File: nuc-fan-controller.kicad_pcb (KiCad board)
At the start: 2 copper layers, 124 x 85 mm, 42 parts, among them J1 19V IN, J2 NUC fan header, J3 FAN 1, J4 FAN 2, J5 Pro Mini, Q1 BC547B, Q2 BC547B, Q3 IRFZ44N, U1 LM2596T, U2 AMS1117-5.0, U3 AMS1117-3.3

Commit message: nuc-fan-controller: the 19V->12V converter is a module now, not parts on the board
Seven parts and their copper — U1 LM2596T-ADJ, L1 100 uH 6 A toroid, D1 1N5822,
C1 220u/35V, C2 100n, R1 1k, RV1 10k trim — are replaced by J6, a 1x04 header
(1,2 GND / 3 19V / 4 +12V) that a finished XL4016E1 step-down module from
cabinet L1 A10 plugs into. C3 470u/25V and C4 stay as the board's local
decoupling where the 12 V rail lands.

This reverses an earlier instruction: the XL4016E1 module had been ruled out and
the converter built from parts instead. The ruling is lifted. BUILD.md says so
out loud and carries the arithmetic that makes the module the better answer at
12 V / 1 A — 5-40 V in, 1.2-36 V out, 8 A, ~180 kHz, ~50 mV ripple; 0.16 A
inductor ripple at this load so it never enters discontinuous conduction and
never pulse-skips; 50 mV of rail ripple attenuated ~5000x by the PWM_IN
divider's time constant. The discrete design is in 10bc262 and every part of it
is still in the cabinet, so the swap goes both ways.

Schematic: 52 wires and 5 junctions, and they are exactly what logs/genwires.py
emits — logs/applywires.py is new and splices that set back into the .kicad_sch.
A pin or a name tag only connects to a wire END, so 19V is written as the segment
chain J1.1 -> (43.18,44.45) -> (48.26,44.45) -> J6.3, the vertices being where
the PWR_FLAG and the name tag hang off it; as one straight wire ERC reports both
as orphaned. ERC: 0 violations.

Board: J6 at (24,34); 19V routed J1 -> (18,34) -> (18,39.08) -> J6.3 and +12V
from J6.4 down and across onto the existing rail; the SW/FB/19V tracks, 22
dangling GND/+12V segments and one stray via deleted; zones refilled; the dead
SW netclass pattern removed; silkscreen beside J6 reads "1,2 GND 3 19V 4 12V".
DRC: 0 violations, 0 unconnected items, and the one documented parity warning —
J2 pin 4's deliberate no-connect.

exports/ rebuilt by logs/export.sh (new): BOM is 32 fitted parts, plus gerbers,
drill, placement, both board plots 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
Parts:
- removed C1: 220uF 35V, Capacitor_THT:CP_Radial_D10.0mm_P5.00mm
- removed C2: 100n, Capacitor_THT:C_Disc_D3.8mm_W2.6mm_P2.50mm
- removed D1: 1N5822, Diode_THT:D_DO-201AD_P15.24mm_Horizontal
- removed L1: 100uH 6A, Inductor_THT:L_Toroid_Horizontal_D16.8mm_P14.70mm_Vishay_TJ3
- removed R1: 1k, Resistor_THT:R_Axial_DIN0204_L3.6mm_D1.6mm_P5.08mm_Horizontal
- removed RV1: 10k trim, Potentiometer_THT:Potentiometer_Bourns_3296W_Vertical
- removed U1: LM2596T, Package_TO_SOT_THT:TO-220-5_P3.4x3.7mm_StaggerOdd_Lead3.8mm_Vertical
- added J6: BUCK MODULE, Connector_PinHeader_2.54mm:PinHeader_1x04_P2.54mm_Vertical, F.Cu at (24.0, 34.0)
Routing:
- net GND: track 333.3 -> 199.5 mm, vias 326 -> 325
- net SW: track 39.6 -> 0.00 mm
- net FB: track 24.5 -> 0.00 mm
- net +12V: track 147.3 -> 166.0 mm
- net 19V: track 31.7 -> 15.1 mm
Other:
- board text added: "1,2 GND 3 19V 4 12V"

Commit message: Wire Q1/Q2 for the BC547s that are actually in the cabinet
The two transistors in R1 D3 are the NXP/Philips order — 1 emitter, 2 base,
3 collector. KiCad's Transistor_BJT:BC547 is the onsemi order (1 C, 2 B, 3 E), so
the schematic, the footprint pad numbers and the parts disagreed. Both symbols are
now Transistor_BJT:Q_NPN_EBC, which draws at identical pin coordinates and differs
only in the pin numbers: nothing on the drawing moved, the nets moved.

schematic (logs/fixq.py)
  Q1/Q2 -> Q_NPN_EBC, Sim.Pins 1=E 2=B 3=C, and the Datasheet link plus the
  Description now state the pinning. ERC 0 violations.

board (logs/fixboard.py, fixboard2.py, fixboard3.py)
  Pad 1 is the emitter on the GND pour, pad 3 the collector. NUC_TACH is re-run
  from Q1 pad 3 around the body onto the tach line at (109.73,18.782); FAN_GATE
  from Q2 pad 3 east to the existing run at (102.969,77.1109). The copper that used
  to hang off the old pads is gone: the GND feeds off Q1.3/Q2.3, the stubs into
  Q1.1/Q2.1, and the orphaned GND feed into R7.2 — R7 takes GND from the pour.
  BASE is jogged to y=74.75 so it clears Q2's now-live pad 1 by 0.40 mm instead of
  0.20, and two stitching vias in the new corridors plus a +12V via with copper on
  one layer only were removed. Silkscreen between the transistors reads
  "Q1 Q2 1=E 2=B 3=C"; pad 1 is the square pad.
  DRC 0 violations, 0 unconnected items, and the documented J2 pin-4 no-connect.

Update-from-schematic also brought in J7 (FAN 1 — the third fan connector) and
C12 100 n on FAN_SW, which were in the schematic but not on the board. J7 sits in
the fan column at (130,76) and is routed with the same bypass style the J3/J4 legs
use. That update had renamed FAN_SW to Net-(C12-Pad1) and PWM_DIV to Net-(R3-Pad2)
on the board, which drops both out of the Power net class, so the names were put
back by hand. BOM is 33 fitted parts.

Docs: BUILD.md gains "Which way round a BC547 goes" — meter them, a BC547B reads
hFE 200-450 forward and single digit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
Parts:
- added J7: FAN 1, Connector_PinHeader_2.54mm:PinHeader_1x02_P2.54mm_Vertical, F.Cu at (130.0, 76.0)
- J3: value FAN 1 -> FAN 2
- J4: value FAN 2 -> FAN 3
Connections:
- Q1 pad 1: NUC_TACH -> GND
- Q1 pad 3: GND -> NUC_TACH
- Q2 pad 1: FAN_GATE -> GND
- Q2 pad 3: GND -> FAN_GATE
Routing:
- net GND: track 199.5 -> 169.4 mm, vias 325 -> 322
- net +12V: track 166.0 -> 182.0 mm
- net NUC_TACH: track 25.8 -> 39.6 mm
- net FAN_SW: track 51.9 -> 63.1 mm
- net FAN_GATE: track 19.7 -> 15.3 mm
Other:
- board text added: "Q1 Q2 1=E 2=B 3=C"

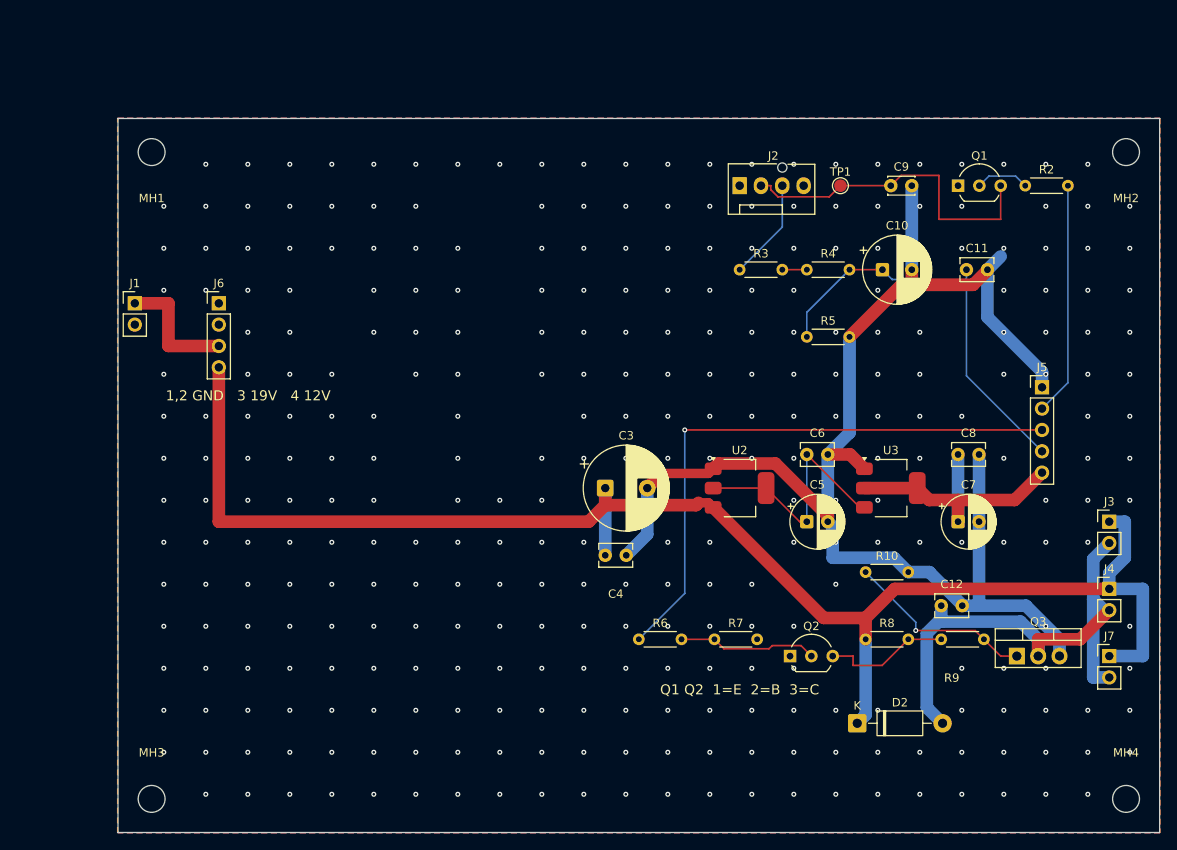
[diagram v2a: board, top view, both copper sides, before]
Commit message: Rebuild the board as one copper layer, 88.90 x 76.20 mm, for home etching
The board is now generated by logs/build1l.py instead of routed by Freerouting: parts,
drawn rails, holes, silkscreen and a small A* for the short legs all live in that script,
with footprint artwork cloned out of the KiCad 10 libraries by logs/getfp.py into
logs/fp-templates.inc.  logs/setrules.py writes the home-etch rules into the project.

Rules: clearance and minimum track 0.70 mm, drawn rails 1.80 mm, copper-to-edge 0.50 mm,
minimum drill 0.90 mm, maximum pad 1.80 mm, pour minimum thickness 0.80 mm.  Every layer
is F.Cu, and F.Cu is the component side, so the copper that gets etched is the copper the
parts solder to and nothing about the board is mirrored.

The ground pour is one island of 5009 mm2 with `connect_pads yes` -- the token matters:
KiCad 10 reads a bare `(connect_pads (clearance 0.7))` as thermal relief and stops the fill
0.70 mm short of every GND pad, which passes DRC and leaves the pads sitting in resin.
Traces of a foreign net keep the pour off, tracks of the pour's own net are absorbed by it,
which is why the router keeps a 2.20 mm gap (2 x clearance + min_thickness) between thin
copper so the fill never gets walled into pockets.

Nets that would fight each other are drawn as bars rather than handed to the router --
+12V, FAN_SW, 19V, +3V3, FAN_PWM, NUC_TACH, NUC_PWM, TACH_OUT, TACH_BASE, PWM_IN -- because
a long leg left to the A* escapes to the board perimeter and walls the pour off.  One
crossing cannot be routed around on a single layer: the Pro Mini's A0 and D11 sit side by
side and their destinations are on opposite sides of the divider row, so R11, a 0 Ohm
bridge, carries FAN_PWM over that row.  R11 is a board part only; the schematic has no such
component, and KiCad's board-only ratsnest therefore reports the join as a missing
connection, which is why that rule is downgraded to a warning and logs/verify.py checks the
real thing instead.

logs/verify.py and logs/p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
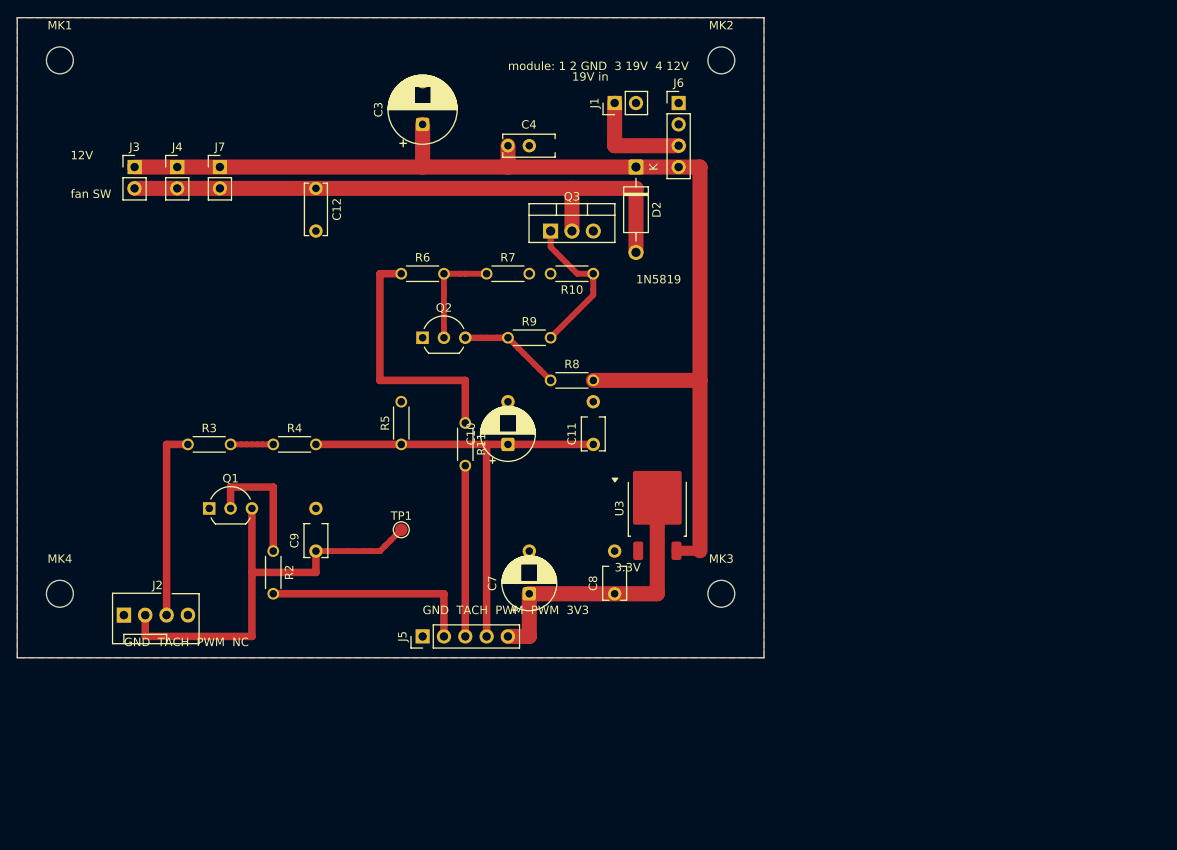
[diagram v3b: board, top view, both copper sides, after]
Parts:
- removed C5: 10uF, Capacitor_THT:CP_Radial_D6.3mm_P2.50mm
- removed C6: 100n, Capacitor_THT:C_Disc_D3.8mm_W2.6mm_P2.50mm
- removed MH1, MH2, MH3, MH4: MountingHole_3.2mm_M3, MountingHole:MountingHole_3.2mm_M3
- removed U2: AMS1117-5.0, Package_TO_SOT_SMD:SOT-223-3_TabPin2
- added MK1: M3, MountingHole:MountingHole_3.2mm_M3, F.Cu at (5.08, 5.08)
- added MK2: M3, MountingHole:MountingHole_3.2mm_M3, F.Cu at (83.8, 5.08)
- added MK3: M3, MountingHole:MountingHole_3.2mm_M3, F.Cu at (83.8, 68.6)
- added MK4: M3, MountingHole:MountingHole_3.2mm_M3, F.Cu at (5.08, 68.6)
- added R11: 0R bridge, Resistor_THT:R_Axial_DIN0204_L3.6mm_D1.6mm_P5.08mm_Horizontal, F.Cu at (53.3, 48.2)
- C10: footprint Capacitor_THT:CP_Radial_D8.0mm_P3.50mm -> Capacitor_THT:CP_Radial_D6.3mm_P2.50mm
- C12, C4: footprint Capacitor_THT:C_Disc_D3.8mm_W2.6mm_P2.50mm -> Capacitor_THT:C_Disc_D6.0mm_W2.5mm_P5.00mm
- C3: footprint Capacitor_THT:CP_Radial_D10.0mm_P5.00mm -> Capacitor_THT:CP_Radial_D8.0mm_P3.50mm
- C9: footprint Capacitor_THT:C_Disc_D3.0mm_W2.0mm_P2.50mm -> Capacitor_THT:C_Disc_D3.8mm_W2.6mm_P2.50mm
- U3: footprint Package_TO_SOT_SMD:SOT-223-3_TabPin2 -> Package_TO_SOT_SMD:TO-252-3_TabPin2
- moved J3 123.5 mm to (14.0, 17.8)
- moved J4 121.8 mm to (19.1, 17.8)
- moved J7 120.8 mm to (24.1, 17.8)
- moved R2 99.5 mm to (30.5, 63.5)
- moved Q1 97.1 mm to (22.9, 58.4)
- moved C12 89.5 mm to (35.6, 20.3)
- moved J2 89.4 mm to (12.7, 71.1)
- moved C9 81.1 mm to (35.6, 63.5)
- moved J5 79.5 mm to (48.3, 73.7)
- moved Q3 75.1 mm to (63.5, 25.4)
- moved D2 71.3 mm to (73.7, 17.8)
- moved R3 68.9 mm to (20.3, 50.8)
- moved R4 66.8 mm to (30.5, 50.8)
- moved TP1 66.4 mm to (45.7, 61.0)
- moved R9 62.8 mm to (58.4, 38.1)
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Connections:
- U3 pad 3: 5V -> +12V
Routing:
- net GND: track 169.4 -> 0.00 mm, vias 322 -> 0
- net +12V: track 182.0 -> 136.1 mm
- net 5V: track 30.3 -> 0.00 mm
- net PWM_IN: track 49.9 -> 76.2 mm
- net FAN_PWM: track 69.7 -> 50.8 mm, vias 1 -> 0
- net NUC_TACH: track 39.6 -> 51.9 mm
- net NUC_PWM: track 12.1 -> 22.9 mm
- net FAN_SW: track 63.1 -> 72.4 mm
- net TACH_BASE: track 6.40 -> 15.2 mm
- net GATE: track 22.7 -> 18.0 mm, vias 1 -> 0
- net BASE: track 16.6 -> 12.7 mm
- net TACH_OUT: track 27.8 -> 25.4 mm
- net 19V: track 15.1 -> 12.7 mm
- net PWM_DIV: track 2.92 -> 5.08 mm
- net FAN_GATE: track 15.3 -> 17.3 mm
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- removed copper zone on B.Cu, net GND
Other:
- board size 124 x 85 mm -> 88.9 x 76.2 mm
- board text added: "12V"
- board text added: "19V in"
- board text added: "1N5819"
- board text added: "3.3V"
- board text added: "GND TACH PWM NC"
- board text added: "GND TACH PWM PWM 3V3"
- board text added: "fan SW"
- board text added: "module: 1 2 GND 3 19V 4 12V"
- board text removed: "1,2 GND 3 19V 4 12V"
- board text removed: "Q1 Q2 1=E 2=B 3=C"
